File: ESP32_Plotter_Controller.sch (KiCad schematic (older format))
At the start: 34 parts, among them J1 ARM JTAG 10pin, J10 Pen Lift, J11 Vselect, J12 X Motor, J13 Y Motor, J14 Neo Pixel LEDs, J15 Pen Direction, J16 Aux Port (I2C), J2 Power, J3 5V Aux, J4 Vin Aux, J5 Limit Switches, J6 Aux Port (SPI), J7 X Limit, J8 Micro_SD_Card, J9 Y Limit, U1 ESP-DEVKITC, U2 TMC2130, U3 TMC2130, U4 XL1509

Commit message: Clean up folder
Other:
- note added: "ESP32 Plotter Controller\nDesign by Mark Benson github.com/markjb/<repo_name>\nBased on Bart Drings ESP32 Pen Plotter Controller\nhttps://github.com/bdring/Grbl_ESP32_TMC2130_Plotter_Controller"
- note removed: "Redesign by Mark Benson\nBased on Bart Drings ESP32\nPen Plotter Controller\nhttps://github.com/bdring/\nGrbl_ESP32_TMC2130_Plotter_Controller"
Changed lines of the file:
@@
 encoding utf-8
 Sheet 1 1
-Title "ESP32 Pen Plotter Controller"
-Date "2021-01-31"
+Title "ESP32 Plotter Controller"
+Date "2021-02-20"
 Rev "0.1"
 Comp ""
 Comment1 ""
-Comment2 "Schematic"
+Comment2 ""
 Comment3 ""
 Comment4 ""
@@
 	1    0    0    -1
 $EndComp
-Text Notes 18900 15375 0    79   ~ 0
-Redesign by Mark Benson\nBased on Bart Drings ESP32\nPen Plotter Controller\nhttps://github.com/bdring/\nGrbl_ESP32_TMC2130_Plotter_Controller
+Text Notes 15050 12575 0    79   ~ 0
+ESP32 Plotter Controller\nDesign by Mark Benson github.com/markjb/<repo_name>\nBased on Bart Drings ESP32 Pen Plotter Controller\nhttps://github.com/bdring/Grbl_ESP32_TMC2130_Plotter_Controller
 Text Label 6530 5300 2    50   ~ 0
 CS_AUX

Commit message: Clean up, add repo name
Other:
- note added: "ESP32 Plotter Controller\nDesign by Mark Benson github.com/markjb/ESP32_Plotter_Controller\nBased on Bart Drings ESP32 Pen Plotter Controller\nhttps://github.com/bdring/Grbl_ESP32_TMC2130_Plotter_Controller"
- note removed: "ESP32 Plotter Controller\nDesign by Mark Benson github.com/markjb/<repo_name>\nBased on Bart Drings ESP32 Pen Plotter Controller\nhttps://github.com/bdring/Grbl_ESP32_TMC2130_Plotter_Controller"
- note removed: "LCSC Part No: C91145"
- note removed: "Moved X_Limit and Y_Limit to input only pins (GPIO34/35) from (GPIO32/GPIO4) respectivley."
- note removed: "Replace the power circuit with something available from jlcpcb (TI TPS54331 maybe? 25cents each...\n\nXL1509-5.0E1 (20 cents each - fixed 5v)"
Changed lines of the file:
@@
 Title "ESP32 Plotter Controller"
 Date "2021-02-20"
-Rev "0.1"
+Rev "A"
 Comp ""
 Comment1 ""
@@
 Text Notes 1050 7460 0    118  ~ 0
 Power
-Text Notes 3050 10485 0    50   ~ 0
-Replace the power circuit with something available from jlcpcb (TI TPS54331 maybe? 25cents each...\n\nXL1509-5.0E1 (20 cents each - fixed 5v)
 $Comp
 L custom:XL1509 U4
@@
 	1    0    0    -1
 $EndComp
-Text Notes 15050 12575 0    79   ~ 0
-ESP32 Plotter Controller\nDesign by Mark Benson github.com/markjb/<repo_name>\nBased on Bart Drings ESP32 Pen Plotter Controller\nhttps://github.com/bdring/Grbl_ESP32_TMC2130_Plotter_Controller
+Text Notes 15000 12575 0    79   ~ 0
+ESP32 Plotter Controller\nDesign by Mark Benson github.com/markjb/ESP32_Plotter_Controller\nBased on Bart Drings ESP32 Pen Plotter Controller\nhttps://github.com/bdring/Grbl_ESP32_TMC2130_Plotter_Controller
 Text Label 6530 5300 2    50   ~ 0
 CS_AUX
@@
 Text Label 10425 7510 2    50   ~ 0
 SDA
-Text Notes 3275 2735 0    50   ~ 0
-Moved X_Limit and Y_Limit to input only pins (GPIO34/35) from (GPIO32/GPIO4) respectivley.
 $Comp
 L power:GND #NetPort06
@@
 Wire Wire Line
 	12475 10260 12475 10460
-Text Notes 10975 10510 0    50   ~ 0
-LCSC Part No: C91145
 Wire Wire Line
 	16750 6085 17500 6085

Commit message: Fix sdcard footprint
Fix mirrored pinout on SD Card footprint.
Also grounded shield in schematic and disconnected the sd insert sense pin from gnd.
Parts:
- removed J8: Micro_SD_Card, custom:HK-TF01A, symbol Connector:Micro_SD_Card
- added J8: Micro_SD_Card_TF-01A, custom:HK-TF01A, symbol custom:Micro_SD_Card_TF-01A
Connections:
- wire segments 207 -> 205
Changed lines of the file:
@@
 	3080 4225 3080 5900
-$Comp
-L Connector:Micro_SD_Card J8
-U 1 1 601FD9BE
-P 11500 9660
-F 0 "J8" H 11450 10377 50  0000 C CNN
-F 1 "Micro_SD_Card" H 11450 10286 50  0000 C CNN
-F 2 "custom:HK-TF01A" H 12650 9960 50  0001 C CNN
-F 3 "http://katalog.we-online.de/em/datasheet/693072010801.pdf" H 11500 9660 50  0001 C CNN
-	1    11500 9660
-	1    0    0    -1
-$EndComp
 $Comp
 L custom:ESP-DEVKITC U1
@@
 	3380 4100 3580 4100
 Wire Wire Line
-	10600 9960 9825 9960
-Wire Wire Line
-	10600 9760 9825 9760
-Wire Wire Line
-	10600 9560 9825 9560
-Wire Wire Line
-	10600 9460 9825 9460
-Text Label 9825 9960 0    50   ~ 0
+	10650 9960 9875 9960
+Wire Wire Line
+	10650 9760 9875 9760
+Wire Wire Line
+	10650 9560 9875 9560
+Wire Wire Line
+	10650 9460 9875 9460
+Text Label 9875 9960 0    50   ~ 0
 MISO
-Text Label 9825 9560 0    50   ~ 0
+Text Label 9875 9560 0    50   ~ 0
 MOSI
-Text Label 9825 9760 0    50   ~ 0
+Text Label 9875 9760 0    50   ~ 0
 SCK
-Text Label 9825 9460 0    50   ~ 0
+Text Label 9875 9460 0    50   ~ 0
 CS_SD
 $Comp
 L power:+3.3V #PWR08
 U 1 1 6025CC95
-P 9575 9235
-F 0 "#PWR08" H 9575 9085 50  0001 C CNN
-F 1 "+3.3V" H 9590 9408 50  0000 C CNN
-F 2 "" H 9575 9235 50  0001 C CNN
-F 3 "" H 9575 9235 50  0001 C CNN
-	1    9575 9235
-	1    0    0    -1
-$EndComp
-Wire Wire Line
-	9575 9660 9575 9235
-Wire Wire Line
-	9575 9660 10600 9660
+P 9625 9235
+F 0 "#PWR08" H 9625 9085 50  0001 C CNN
+F 1 "+3.3V" H 9640 9408 50  0000 C CNN
+F 2 "" H 9625 9235 50  0001 C CNN
+F 3 "" H 9625 9235 50  0001 C CNN
+	1    9625 9235
+	1    0    0    -1
+$EndComp
+Wire Wire Line
+	9625 9660 9625 9235
+Wire Wire Line
+	9625 9660 10650 9660
 $Comp
 L power:GND #NetPort08
 U 1 1 602713A8
-P 9575 10235
-F 0 "#NetPort08" H 9575 10235 50  0001 C CNN
-F 1 "GND" H 9575 10235 50  0001 C CNN
-F 2 "" H 9575 10235 50  0001 C CNN
-F 3 "" H 9575 10235 50  0001 C CNN
-	1    9575 10235
-	1    0    0    -1
-$EndComp
-Wire Wire Line
-	9575 9860 9575 10235
-Wire Wire Line
-	9575 9860 10600 9860
-$Comp
-L power:GND #NetPort09
-U 1 1 602859AC
-P 12475 10460
-F 0 "#NetPort09" H 12475 10460 50  0001 C CNN
-F 1 "GND" H 12475 10460 50  0001 C CNN
-F 2 "" H 12475 10460 50  0001 C CNN
-F 3 "" H 12475 10460 50  0001 C CNN
-	1    12475 10460
-	1    0    0    -1
-$EndComp
-Wire Wire Line
-	12300 10260 12475 10260
-Wire Wire Line
-	12475 10260 12475 10460
+P 9625 10235
+F 0 "#NetPort08" H 9625 10235 50  0001 C CNN
+F 1 "GND" H 9625 10235 50  0001 C CNN
+F 2 "" H 9625 10235 50  0001 C CNN
+F 3 "" H 9625 10235 50  0001 C CNN
+	1    9625 10235
+	1    0    0    -1
+$EndComp
+Wire Wire Line
+	9625 9860 9625 10235
+Wire Wire Line
+	9625 9860 10650 9860
 Wire Wire Line
 	16750 6085 17500 6085
@@
 	1    0    0    -1
 $EndComp
+$Comp
+L custom:Micro_SD_Card_TF-01A J8
+U 1 1 6071C640
+P 11550 9660
+F 0 "J8" H 12380 9656 50  0000 L CNN
+F 1 "Micro_SD_Card_TF-01A" H 12380 9565 50  0000 L CNN
+F 2 "custom:HK-TF01A" H 12700 9960 50  0001 C CNN
+F 3 "http://katalog.we-online.de/em/datasheet/693072010801.pdf" H 11550 9660 50  0001 C CNN
+	1    11550 9660
+	1    0    0    -1
+$EndComp
+$Comp
+L power:GND #PWR0101
+U 1 1 60748F7B
+P 12000 10460
+F 0 "#PWR0101" H 12000 10210 50  0001 C CNN
+F 1 "GND" H 12005 10287 50  0000 C CNN
+F 2 "" H 12000 10460 50  0001 C CNN
+F 3 "" H 12000 10460 50  0001 C CNN
+	1    12000 10460
+	1    0    0    -1
+$EndComp
+$Comp
+L power:GND #PWR0102
+U 1 1 6074955A
+P 11150 10460
+F 0 "#PWR0102" H 11150 10210 50  0001 C CNN
+F 1 "GND" H 11155 10287 50  0000 C CNN
+F 2 "" H 11150 10460 50  0001 C CNN
+F 3 "" H 11150 10460 50  0001 C CNN
+	1    11150 10460
+	1    0    0    -1
+$EndComp
+$Comp
+L power:GND #PWR0103
+U 1 1 6074A18C
+P 11150 8960
+F 0 "#PWR0103" H 11150 8710 50  0001 C CNN
+F 1 "GND" H 11155 8787 50  0000 C CNN
+F 2 "" H 11150 8960 50  0001 C CNN
+F 3 "" H 11150 8960 50  0001 C CNN
+	1    11150 8960
+	-1   0    0    1
+$EndComp
+$Comp
+L power:GND #PWR0104
+U 1 1 6074AC3D
+P 12000 8960
+F 0 "#PWR0104" H 12000 8710 50  0001 C CNN
+F 1 "GND" H 12005 8787 50  0000 C CNN
+F 2 "" H 12000 8960 50  0001 C CNN
+F 3 "" H 12000 8960 50  0001 C CNN
+	1    12000 8960
+	-1   0    0    1
+$EndComp
 $EndSCHEMATC

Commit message: Use ESP32 module and CH340C for comms
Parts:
- removed D1: B5819W, Diode_SMD:D_SOD-123, symbol Device:D_Schottky
- removed U1: ESP-DEVKITC, custom:DEVKITC, symbol custom:ESP-DEVKITC
- added C10, C9: 22uF 10v, symbol Device:CP
- added C11, C8: 0.1uF, symbol Device:C
- added J17: USB_B_Micro, symbol Connector:USB_B_Micro
- added SW1: RESET, symbol Switch:SW_Push
- added SW2: BOOT, symbol Switch:SW_Push
- added U1: ESP32-WROOM-32D, RF_Module:ESP32-WROOM-32, symbol custom:ESP32-WROOM-32D
- added U5: CH340C, Package_SO:SOIC-16_3.9x9.9mm_P1.27mm, symbol Interface_USB:CH340C
- added U6: AMS1117-3.3, Package_TO_SOT_SMD:SOT-223-3_TabPin2, symbol Regulator_Linear:AMS1117-3.3
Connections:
- net +3V3: now also C10.1, U1.2 (3v3), U5.16 (VCC), U5.4 (V3), U6.2 (VO)
- net +5V: now also C9.1, U6.3 (VI)
- net CS_AUX: now also U1.26 (IO4)
- net CS_SD: now also U1.29 (IO5)
- net CS_X: now also U1.28 (IO17)
- net CS_Y: now also U1.27 (IO16)
- net GND: now also C10.2, C11.2, C8.1, C9.2, J17.5 (GND), SW1.1, SW2.1, U1.1 (GND), U1.15 (GND), U1.38 (GND), U5.1 (GND), U6.1 (GND)
- net JTAG_TDI: now also U1.14 (IO12)
- net JTAG_TMS: now also U1.13 (IO14)
- net MISO: now also U1.31 (IO19)
- net MOSI: now also U1.37 (IO23)
- net NEO_PIXELS_JTAG_TCK: now also U1.16 (IO13)
- net PEN_DIR_JTAG_TDO: now also U1.23 (IO15)
- net PEN_LIFT: now also U1.12 (IO27)
- net SCK: now also U1.30 (IO18)
- net SCL: now also U1.36 (IO22)
- net SDA: now also U1.33 (IO21)
- net StepEn: now also U1.24 (IO2)
- net X_Dir: now also U1.11 (IO26)
- net X_Limit: now also U1.6 (IO34)
- net X_Step: now also U1.10 (IO25)
- net Y_Dir: now also U1.9 (IO33)
- net Y_Limit: now also U1.7 (IO35)
- net Y_Step: now also U1.8 (IO32)
- new net: J17.3 (D+), U5.5 (UD+)
- new net: J17.2 (D-), U5.6 (UD-)
- new net EN: C8.2, SW1.2, U1.3 (EN)
- new net ESP32_RX: U1.34 (RXD0), U5.2 (TXD)
- new net ESP32_TX: U1.35 (TXD0), U5.3 (RXD)
- new net IO0: C11.1, SW2.2, U1.25 (IO0)
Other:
- note added: "Comms"
- note removed: "LCSC: C8598"
- moved on the sheet: C1, C2, C3, C4, C5, C6, C7, D2, J1, J10, J11, J12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

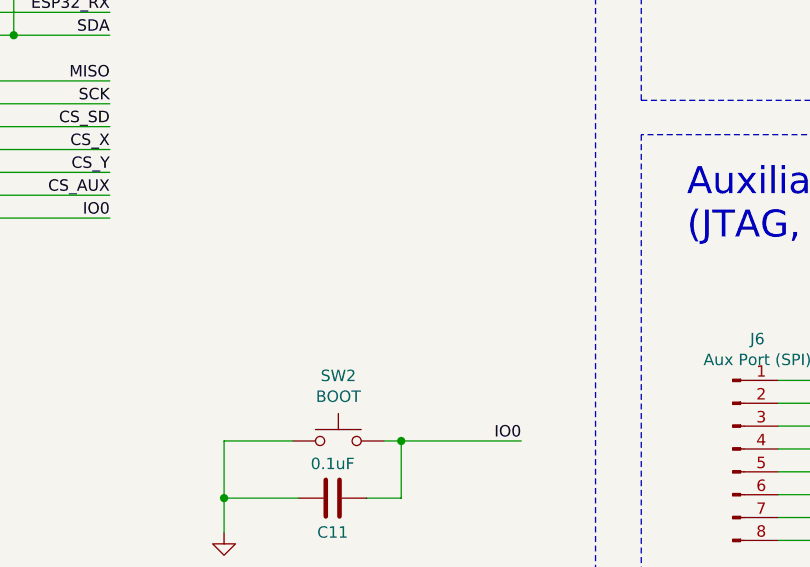
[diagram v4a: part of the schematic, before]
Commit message: Associate footprints
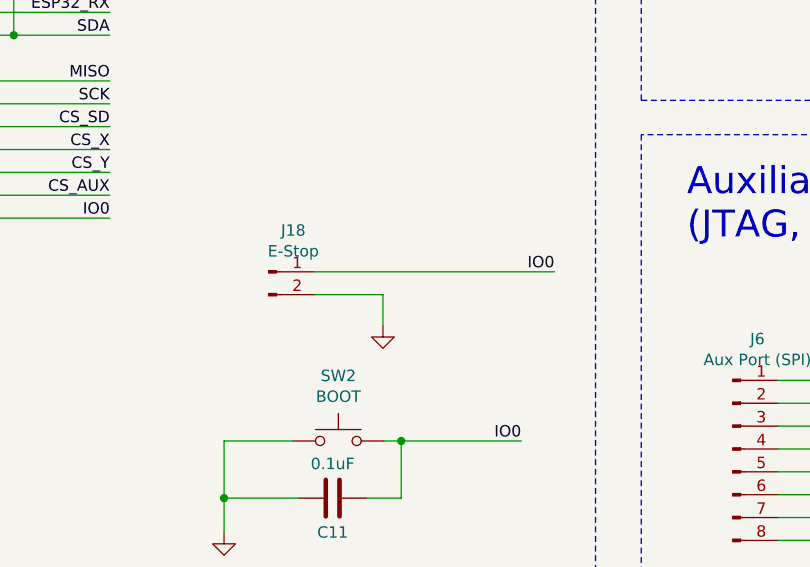
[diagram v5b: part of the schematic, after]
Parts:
- added J18: E-Stop, Connector_PinHeader_2.54mm:PinHeader_1x02_P2.54mm_Vertical, symbol Connector:Conn_01x02_Male
- C10, C9: footprint (none) -> Capacitor_Tantalum_SMD:CP_EIA-3216-10_Kemet-I; LCSC (none) -> C118989
- C11, C8: footprint (none) -> Capacitor_SMD:C_0603_1608Metric
- J17: footprint (none) -> Connector_USB:USB_Micro-B_Molex-105017-0001; LCSC (none) -> C381143
- SW1, SW2: footprint (none) -> Button_Switch_SMD:SW_SPST_EVQP2; LCSC (none) -> C512395
- U5: LCSC (none) -> C84681
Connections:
- net GND: now also J18.2 (Pin_2)
- net IO0: now also J18.1 (Pin_1)
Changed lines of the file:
@@
 Title "ESP32 Plotter Controller"
 Date "2021-02-20"
-Rev "A"
+Rev "B"
 Comp ""
 Comment1 ""
@@
 F 0 "C9" H 5743 8746 50  0000 L CNN
 F 1 "22uF 10v" H 5743 8655 50  0000 L CNN
-F 2 "" H 5663 8550 50  0001 C CNN
+F 2 "Capacitor_Tantalum_SMD:CP_EIA-3216-10_Kemet-I" H 5663 8550 50  0001 C CNN
 F 3 "~" H 5625 8700 50  0001 C CNN
+F 4 "C118989" H 5625 8700 50  0001 C CNN "LCSC"
 	1    5625 8700
 	1    0    0    -1
@@
 F 0 "C10" H 7143 8746 50  0000 L CNN
 F 1 "22uF 10v" H 7143 8655 50  0000 L CNN
-F 2 "" H 7063 8550 50  0001 C CNN
+F 2 "Capacitor_Tantalum_SMD:CP_EIA-3216-10_Kemet-I" H 7063 8550 50  0001 C CNN
 F 3 "~" H 7025 8700 50  0001 C CNN
+F 4 "C118989" H 7025 8700 50  0001 C CNN "LCSC"
 	1    7025 8700
 	1    0    0    -1
@@
 F 2 "Package_SO:SOIC-16_3.9x9.9mm_P1.27mm" H 4375 11100 50  0001 L CNN
 F 3 "https://datasheet.lcsc.com/szlcsc/Jiangsu-Qin-Heng-CH340C_C84681.pdf" H 3975 12450 50  0001 C CNN
+F 4 "C84681" H 4325 11650 50  0001 C CNN "LCSC"
 	1    4325 11650
 	1    0    0    -1
@@
 F 0 "J17" H 2907 12017 50  0000 C CNN
 F 1 "USB_B_Micro" H 2907 11926 50  0000 C CNN
-F 2 "" H 3000 11500 50  0001 C CNN
+F 2 "Connector_USB:USB_Micro-B_Molex-105017-0001" H 3000 11500 50  0001 C CNN
 F 3 "~" H 3000 11500 50  0001 C CNN
+F 4 "C381143" H 2850 11550 50  0001 C CNN "LCSC"
 	1    2850 11550
 	1    0    0    -1
@@
 F 0 "SW1" H 2000 4535 50  0000 C CNN
 F 1 "RESET" H 2000 4444 50  0000 C CNN
-F 2 "" H 2000 4450 50  0001 C CNN
+F 2 "Button_Switch_SMD:SW_SPST_EVQP2" H 2000 4450 50  0001 C CNN
 F 3 "~" H 2000 4450 50  0001 C CNN
+F 4 "C512395" H 2000 4250 50  0001 C CNN "LCSC"
 	1    2000 4250
 	1    0    0    -1
@@
 F 0 "SW2" H 7325 4535 50  0000 C CNN
 F 1 "BOOT" H 7325 4444 50  0000 C CNN
-F 2 "" H 7325 4450 50  0001 C CNN
+F 2 "Button_Switch_SMD:SW_SPST_EVQP2" H 7325 4450 50  0001 C CNN
 F 3 "~" H 7325 4450 50  0001 C CNN
+F 4 "C512395" H 7325 4250 50  0001 C CNN "LCSC"
 	1    7325 4250
 	1    0    0    -1
@@
 F 0 "C11" V 7450 4500 50  0000 C CNN
 F 1 "0.1uF" V 7150 4500 50  0000 C CNN
-F 2 "" H 7338 4350 50  0001 C CNN
+F 2 "Capacitor_SMD:C_0603_1608Metric" H 7338 4350 50  0001 C CNN
 F 3 "~" H 7300 4500 50  0001 C CNN
 	1    7300 4500
@@
 F 0 "C8" V 1800 4500 50  0000 C CNN
 F 1 "0.1uF" V 2125 4500 50  0000 C CNN
-F 2 "" H 2013 4350 50  0001 C CNN
+F 2 "Capacitor_SMD:C_0603_1608Metric" H 2013 4350 50  0001 C CNN
 F 3 "~" H 1975 4500 50  0001 C CNN
 	1    1975 4500
@@
 Text Label 2625 4250 2    50   ~ 0
 EN
+$Comp
+L Connector:Conn_01x02_Male J18
+U 1 1 61ACBD71
+P 7020 3510
+F 0 "J18" H 7128 3691 50  0000 C CNN
+F 1 "E-Stop" H 7128 3600 50  0000 C CNN
+F 2 "Connector_PinHeader_2.54mm:PinHeader_1x02_P2.54mm_Vertical" H 7020 3510 50  0001 C CNN
+F 3 "~" H 7020 3510 50  0001 C CNN
+	1    7020 3510
+	1    0    0    -1
+$EndComp
+Wire Wire Line
+	7220 3610 7520 3610
+Wire Wire Line
+	7220 3510 8270 3510
+Wire Wire Line
+	7520 3745 7520 3610
+Text Label 8270 3510 2    50   ~ 0
+IO0
+$Comp
+L power:GND #NetPort014
+U 1 1 61ACC537
+P 7520 3745
+F 0 "#NetPort014" H 7520 3745 50  0001 C CNN
+F 1 "GND" H 7520 3745 50  0001 C CNN
+F 2 "" H 7520 3745 50  0001 C CNN
+F 3 "" H 7520 3745 50  0001 C CNN
+	1    7520 3745
+	1    0    0    -1
+$EndComp
 $EndSCHEMATC

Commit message: Updated component association
Lost some footprint associations, but also changed some footprints to use alternative components from LCSC
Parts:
- C10, C9: footprint Capacitor_Tantalum_SMD:CP_EIA-3216-10_Kemet-I -> Capacitor_Tantalum_SMD:CP_EIA-3216-18_Kemet-A
- J18: footprint Connector_PinHeader_2.54mm:PinHeader_1x02_P2.54mm_Vertical -> Connector_PinHeader_2.54mm:PinHeader_1x02_P2.54mm_Horizontal
- SW1: footprint Button_Switch_SMD:SW_SPST_EVQP2 -> Button_Switch_SMD:SW_SPST_B3S-1000; LCSC C512395 -> C127509
- SW2: footprint Button_Switch_SMD:SW_SPST_EVQP2 -> Button_Switch_SMD:SW_SPST_B3S-1000; LCSC C512395 -> (none)
- U5: LCSC C84681 -> (none)
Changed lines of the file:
@@
 F 0 "C9" H 5743 8746 50  0000 L CNN
 F 1 "22uF 10v" H 5743 8655 50  0000 L CNN
-F 2 "Capacitor_Tantalum_SMD:CP_EIA-3216-10_Kemet-I" H 5663 8550 50  0001 C CNN
+F 2 "Capacitor_Tantalum_SMD:CP_EIA-3216-18_Kemet-A" H 5663 8550 50  0001 C CNN
 F 3 "~" H 5625 8700 50  0001 C CNN
 F 4 "C118989" H 5625 8700 50  0001 C CNN "LCSC"
@@
 F 0 "C10" H 7143 8746 50  0000 L CNN
 F 1 "22uF 10v" H 7143 8655 50  0000 L CNN
-F 2 "Capacitor_Tantalum_SMD:CP_EIA-3216-10_Kemet-I" H 7063 8550 50  0001 C CNN
+F 2 "Capacitor_Tantalum_SMD:CP_EIA-3216-18_Kemet-A" H 7063 8550 50  0001 C CNN
 F 3 "~" H 7025 8700 50  0001 C CNN
 F 4 "C118989" H 7025 8700 50  0001 C CNN "LCSC"
@@
 F 2 "Package_SO:SOIC-16_3.9x9.9mm_P1.27mm" H 4375 11100 50  0001 L CNN
 F 3 "https://datasheet.lcsc.com/szlcsc/Jiangsu-Qin-Heng-CH340C_C84681.pdf" H 3975 12450 50  0001 C CNN
-F 4 "C84681" H 4325 11650 50  0001 C CNN "LCSC"
 	1    4325 11650
 	1    0    0    -1
@@
 F 0 "SW1" H 2000 4535 50  0000 C CNN
 F 1 "RESET" H 2000 4444 50  0000 C CNN
-F 2 "Button_Switch_SMD:SW_SPST_EVQP2" H 2000 4450 50  0001 C CNN
-F 3 "~" H 2000 4450 50  0001 C CNN
-F 4 "C512395" H 2000 4250 50  0001 C CNN "LCSC"
+F 2 "Button_Switch_SMD:SW_SPST_B3S-1000" H 2000 4450 50  0001 C CNN
+F 3 "https://datasheet.lcsc.com/lcsc/1811082113_Korean-Hroparts-Elec-K2-1102SP-C4SC-04_C127509.pdf" H 2000 4450 50  0001 C CNN
+F 4 "C127509" H 2000 4250 50  0001 C CNN "LCSC"
 	1    2000 4250
 	1    0    0    -1
@@
 F 0 "SW2" H 7325 4535 50  0000 C CNN
 F 1 "BOOT" H 7325 4444 50  0000 C CNN
-F 2 "Button_Switch_SMD:SW_SPST_EVQP2" H 7325 4450 50  0001 C CNN
+F 2 "Button_Switch_SMD:SW_SPST_B3S-1000" H 7325 4450 50  0001 C CNN
 F 3 "~" H 7325 4450 50  0001 C CNN
-F 4 "C512395" H 7325 4250 50  0001 C CNN "LCSC"
 	1    7325 4250
 	1    0    0    -1
@@
 F 0 "J18" H 7128 3691 50  0000 C CNN
 F 1 "E-Stop" H 7128 3600 50  0000 C CNN
-F 2 "Connector_PinHeader_2.54mm:PinHeader_1x02_P2.54mm_Vertical" H 7020 3510 50  0001 C CNN
+F 2 "Connector_PinHeader_2.54mm:PinHeader_1x02_P2.54mm_Horizontal" H 7020 3510 50  0001 C CNN
 F 3 "~" H 7020 3510 50  0001 C CNN
 	1    7020 3510
